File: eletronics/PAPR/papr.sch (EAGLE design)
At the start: 6 parts

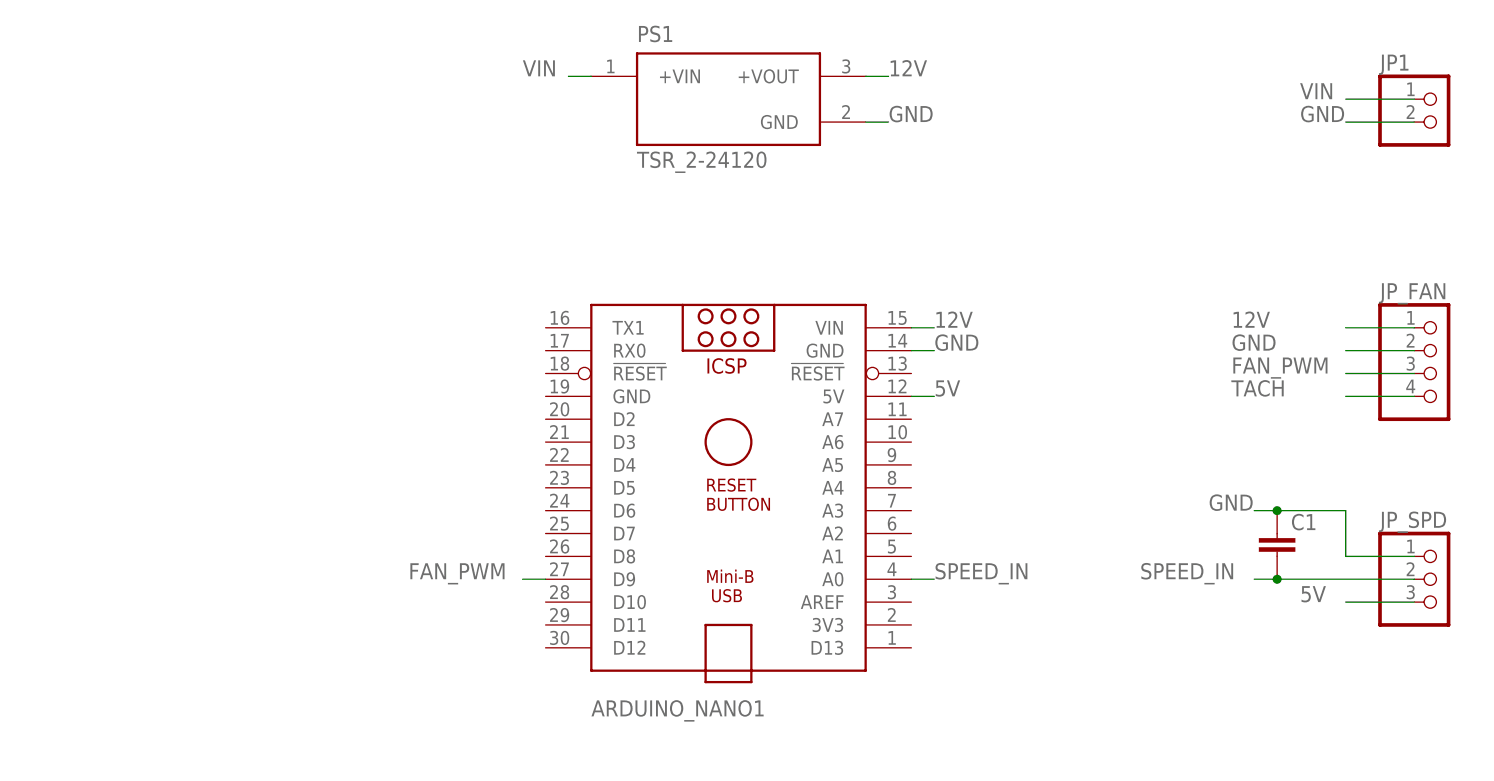
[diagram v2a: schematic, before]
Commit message: Added pullup resistor
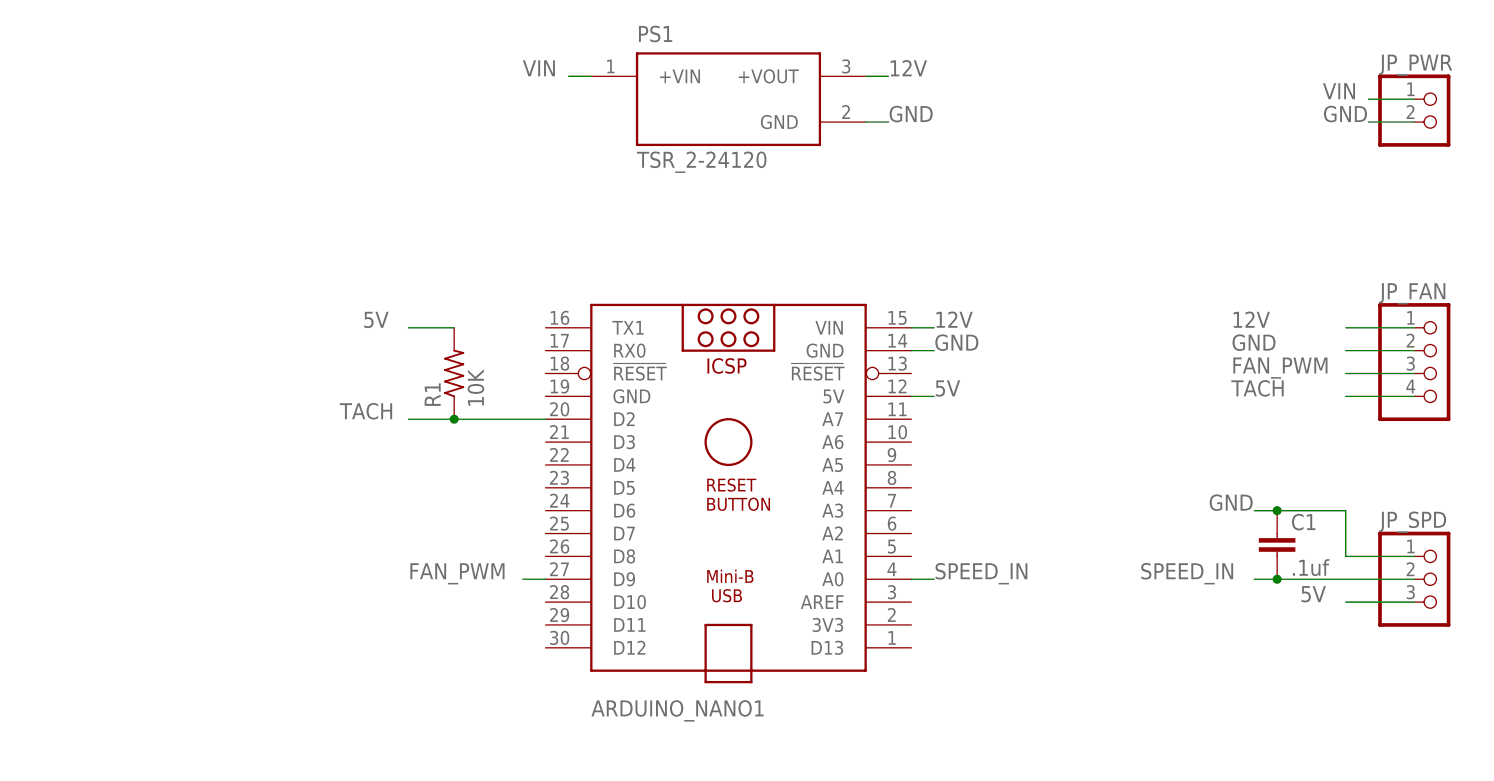
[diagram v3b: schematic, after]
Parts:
- added R1: 10K, rcl:R-US_0204/5
- C1: value (none) -> .1uf
- renumbered JP1 to JP_PWR
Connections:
- net 5V: now also R1.2
- net TACH: now also ARDUINO_NANO1.D2, R1.1
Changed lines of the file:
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@@
 <part name="JP_FAN" library="pinhead" library_urn="urn:adsk.eagle:library:325" deviceset="PINHD-1X4" device="" package3d_urn="urn:adsk.eagle:package:22407/2"/>
 <part name="JP_SPD" library="pinhead" library_urn="urn:adsk.eagle:library:325" deviceset="PINHD-1X3" device="" package3d_urn="urn:adsk.eagle:package:22458/2"/>
-<part name="C1" library="capacitor-wima" library_urn="urn:adsk.eagle:library:116" deviceset="C" device="2,5-3" package3d_urn="urn:adsk.eagle:package:5436/1"/>
-<part name="JP1" library="pinhead" library_urn="urn:adsk.eagle:library:325" deviceset="PINHD-1X2" device="" package3d_urn="urn:adsk.eagle:package:22435/2"/>
+<part name="C1" library="capacitor-wima" library_urn="urn:adsk.eagle:library:116" deviceset="C" device="2,5-3" package3d_urn="urn:adsk.eagle:package:5436/1" value=".1uf"/>
+<part name="JP_PWR" library="pinhead" library_urn="urn:adsk.eagle:library:325" deviceset="PINHD-1X2" device="" package3d_urn="urn:adsk.eagle:package:22435/2"/>
+<part name="R1" library="rcl" library_urn="urn:adsk.eagle:library:334" deviceset="R-US_" device="0204/5" package3d_urn="urn:adsk.eagle:package:23488/1" value="10K"/>
 </parts>
 <sheets>
@@
 <attribute name="VALUE" x="113.284" y="48.641" size="1.778" layer="96"/>
 </instance>
-<instance part="JP1" gate="G$1" x="129.54" y="99.06" smashed="yes">
+<instance part="JP_PWR" gate="G$1" x="129.54" y="99.06" smashed="yes">
 <attribute name="NAME" x="123.19" y="104.775" size="1.778" layer="95"/>
 <attribute name="VALUE" x="123.19" y="93.98" size="1.778" layer="96"/>
+</instance>
+<instance part="R1" gate="G$1" x="20.32" y="71.12" smashed="yes" rot="R90">
+<attribute name="NAME" x="18.8214" y="67.31" size="1.778" layer="95" rot="R90"/>
+<attribute name="VALUE" x="23.622" y="67.31" size="1.778" layer="96" rot="R90"/>
 </instance>
 </instances>
@@
 </segment>
 <segment>
+<pinref part="JP_FAN" gate="A" pin="1"/>
+<wire x1="127" y1="76.2" x2="119.38" y2="76.2" width="0.1524" layer="91"/>
+<label x="106.68" y="76.2" size="1.778" layer="95"/>
+</segment>
+<segment>
 <pinref part="PS1" gate="G$1" pin="+VOUT"/>
 <wire x1="66.04" y1="104.14" x2="68.58" y2="104.14" width="0.1524" layer="91"/>
 <label x="68.58" y="104.14" size="1.778" layer="95"/>
 </segment>
-<segment>
-<pinref part="JP_FAN" gate="A" pin="1"/>
-<wire x1="127" y1="76.2" x2="119.38" y2="76.2" width="0.1524" layer="91"/>
-<label x="106.68" y="76.2" size="1.778" layer="95"/>
-</segment>
 </net>
 <net name="GND" class="0">
-<segment>
-<pinref part="PS1" gate="G$1" pin="GND"/>
-<wire x1="66.04" y1="99.06" x2="68.58" y2="99.06" width="0.1524" layer="91"/>
-<label x="68.58" y="99.06" size="1.778" layer="95"/>
-</segment>
 <segment>
 <pinref part="ARDUINO_NANO1" gate="G$1" pin="GND@2"/>
@@
 </segment>
 <segment>
-<pinref part="JP1" gate="G$1" pin="2"/>
-<wire x1="127" y1="99.06" x2="119.38" y2="99.06" width="0.1524" layer="91"/>
-<label x="114.3" y="99.06" size="1.778" layer="95"/>
-</segment>
-</net>
-<net name="VIN" class="0">
-<segment>
-<pinref part="PS1" gate="G$1" pin="+VIN"/>
-<wire x1="35.56" y1="104.14" x2="33.02" y2="104.14" width="0.1524" layer="91"/>
-<label x="27.94" y="104.14" size="1.778" layer="95"/>
+<pinref part="JP_PWR" gate="G$1" pin="2"/>
+<wire x1="127" y1="99.06" x2="121.92" y2="99.06" width="0.1524" layer="91"/>
+<label x="116.84" y="99.06" size="1.778" layer="95"/>
 </segment>
 <segment>
-<pinref part="JP1" gate="G$1" pin="1"/>
-<wire x1="127" y1="101.6" x2="119.38" y2="101.6" width="0.1524" layer="91"/>
-<label x="114.3" y="101.6" size="1.778" layer="95"/>
+<pinref part="PS1" gate="G$1" pin="GND"/>
+<wire x1="66.04" y1="99.06" x2="68.58" y2="99.06" width="0.1524" layer="91"/>
+<label x="68.58" y="99.06" size="1.778" layer="95"/>
 </segment>
 </net>
@@
 <label x="106.68" y="68.58" size="1.778" layer="95"/>
 </segment>
+<segment>
+<pinref part="ARDUINO_NANO1" gate="G$1" pin="D2"/>
+<wire x1="30.48" y1="66.04" x2="20.32" y2="66.04" width="0.1524" layer="91"/>
+<label x="7.62" y="66.04" size="1.778" layer="95"/>
+<pinref part="R1" gate="G$1" pin="1"/>
+<wire x1="20.32" y1="66.04" x2="15.24" y2="66.04" width="0.1524" layer="91"/>
+<junction x="20.32" y="66.04"/>
+</segment>
 </net>
 <net name="5V" class="0">
@@
 <label x="73.66" y="68.58" size="1.778" layer="95"/>
 </segment>
+<segment>
+<wire x1="20.32" y1="76.2" x2="15.24" y2="76.2" width="0.1524" layer="91"/>
+<label x="10.16" y="76.2" size="1.778" layer="95"/>
+<pinref part="R1" gate="G$1" pin="2"/>
+</segment>
+</net>
+<net name="VIN" class="0">
+<segment>
+<pinref part="PS1" gate="G$1" pin="+VIN"/>
+<wire x1="35.56" y1="104.14" x2="33.02" y2="104.14" width="0.1524" layer="91"/>
+<label x="27.94" y="104.14" size="1.778" layer="95"/>
+</segment>
+<segment>
+<pinref part="JP_PWR" gate="G$1" pin="1"/>
+<wire x1="127" y1="101.6" x2="121.92" y2="101.6" width="0.1524" layer="91"/>
+<label x="116.84" y="101.6" size="1.778" layer="95"/>
+</segment>
 </net>
 </nets>
 </sheet>
 </sheets>
+<errors>
+</errors>
 </schematic>
 </drawing>
@@
 packages will not be understood (or retained) with this version.
 </note>
+<note version="8.4" severity="warning">
+Since Version 8.4, EAGLE supports properties for SPICE simulation.
+Probes in schematics and SPICE mapping objects found in parts and library devices
+will not be understood with this version. Update EAGLE to the latest version
+for full support of SPICE simulation.
+</note>
 </compatibility>
